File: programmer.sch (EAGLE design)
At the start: 23 parts, among them IC1 74241, U1 ATMEGA8U2, X2 SPARKFUN_USB-MICROB, Y1 16MHz

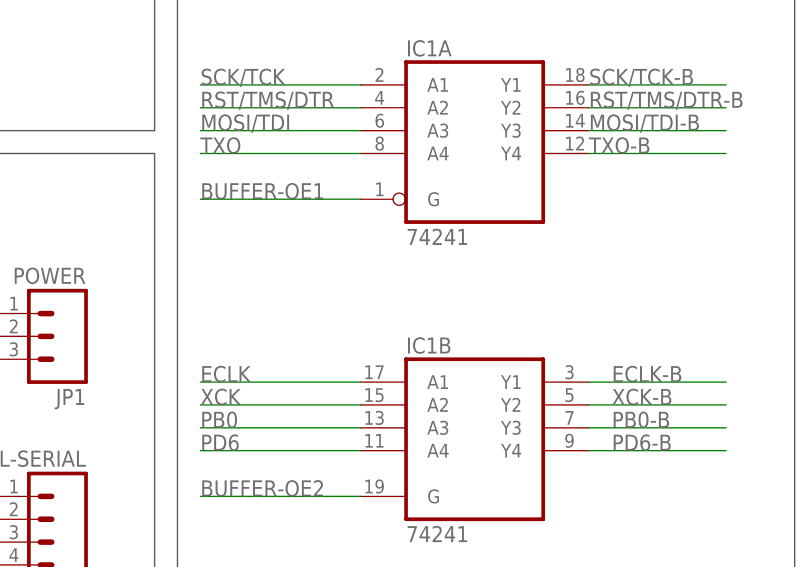
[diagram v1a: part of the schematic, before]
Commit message: Add note about substituting '244.
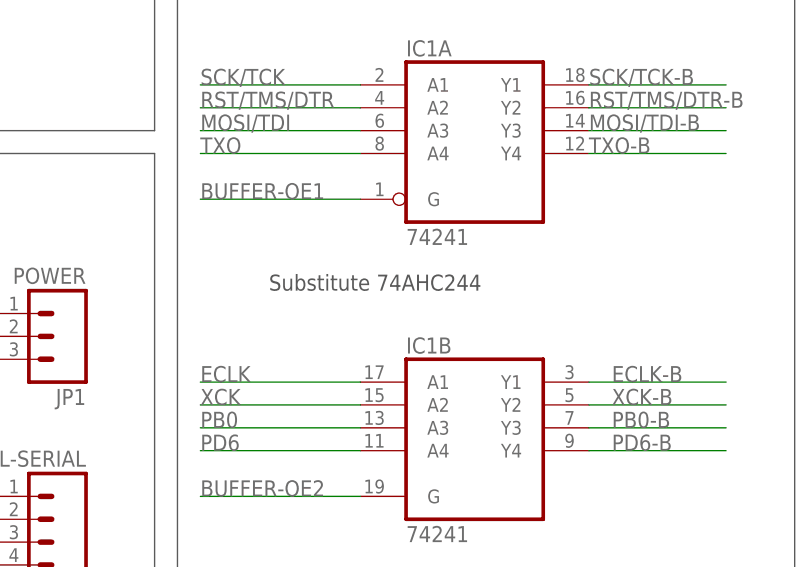
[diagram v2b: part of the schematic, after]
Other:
- note added: "Substitute 74AHC244"
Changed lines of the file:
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@@
 <text x="10.16" y="132.08" size="5.08" layer="97" font="vector">ATmegaXXU2</text>
 <text x="15.24" y="-27.94" size="1.778" layer="97" font="vector">Micro USB connector might not exist in real life</text>
+<text x="109.22" y="38.1" size="1.778" layer="97" font="vector">Substitute 74AHC244</text>
 </plain>
 <instances>

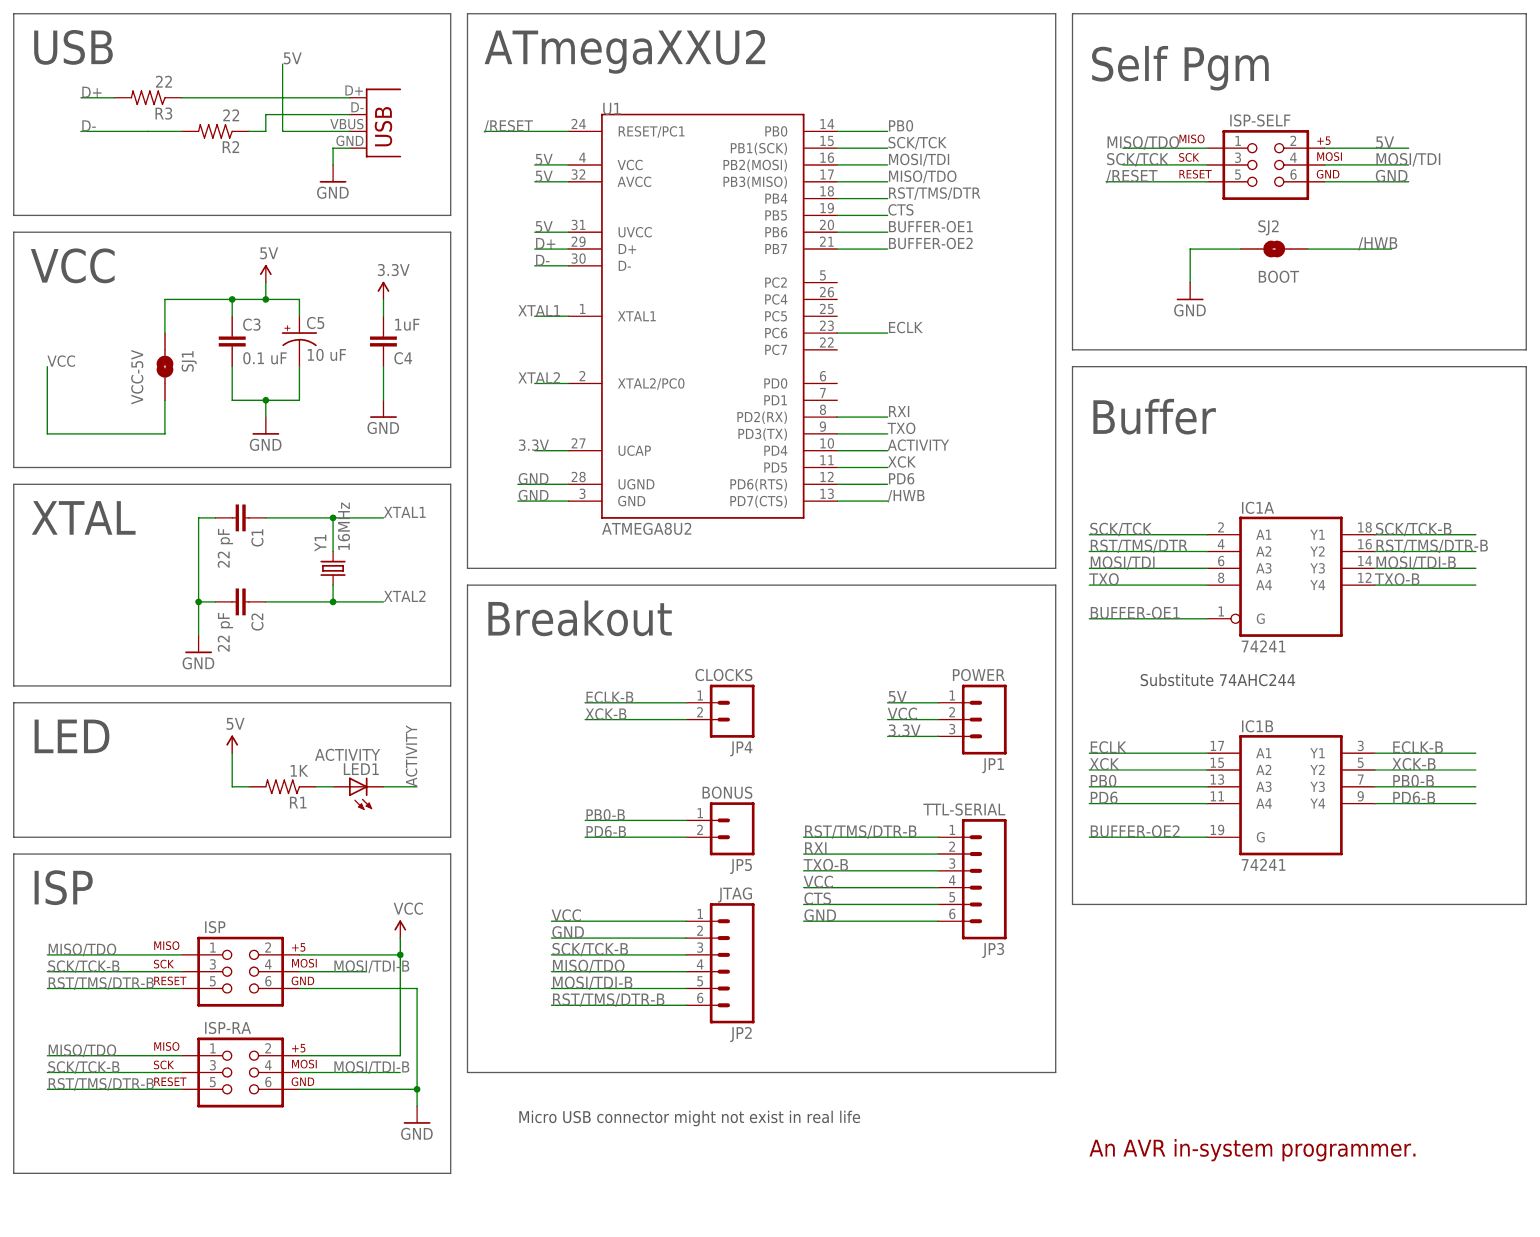
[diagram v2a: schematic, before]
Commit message: Various changes.
- Change VCC labels to VIO (https://github.com/sowbug/avr-programmer/issues/15).
- Change LED resistor from 1K to 330 (https://github.com/sowbug/avr-programmer/issues/16).
- Added second status LED (https://github.com/sowbug/avr-programmer/issues/9).
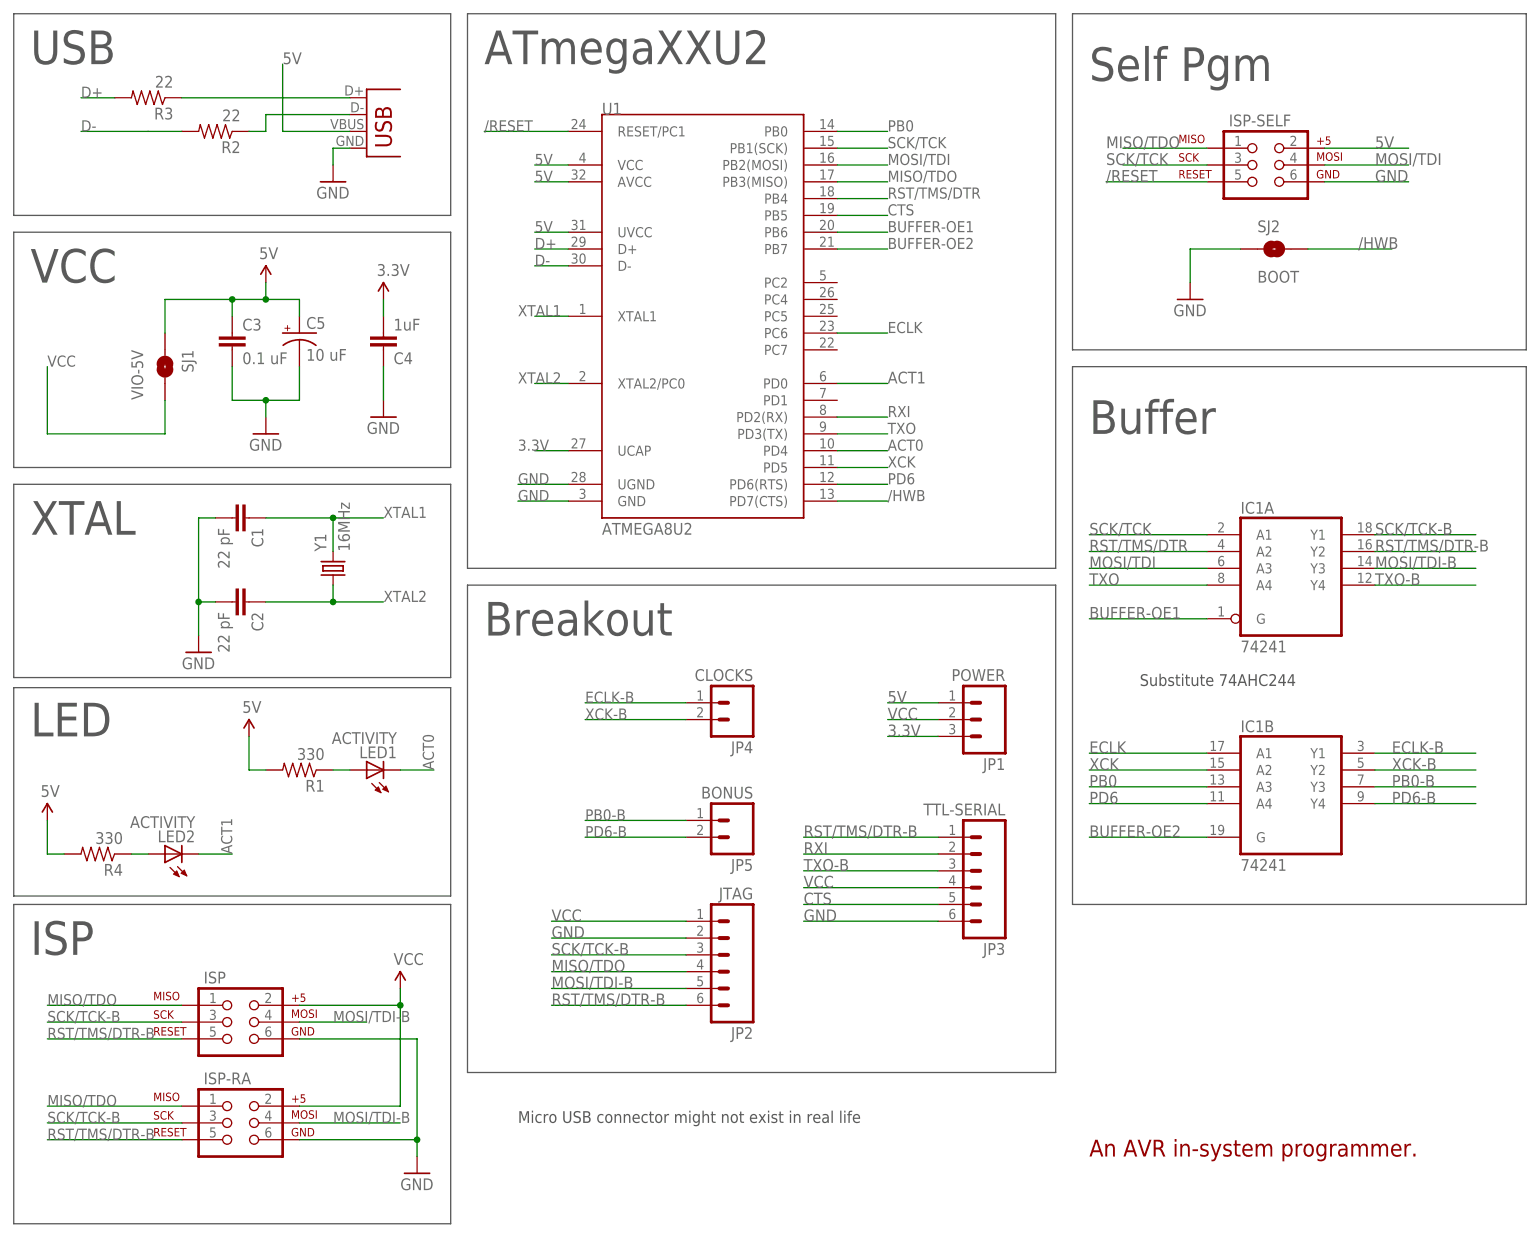
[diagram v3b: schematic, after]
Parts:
- added LED2: ACTIVITY, programmer:SPARKFUN_LED
- added R4: 330, programmer:SPARKFUN_RESISTOR0805-RES
- R1: value 1K -> 330
- SJ1: value VCC-5V -> VIO-5V
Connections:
- net ACTIVITY renamed ACT0
- new net ACT1: LED2.C, U1.PD0
- new net VCC-LED1: LED2.A, R4.1
- net 5V: now also R4.2
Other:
- moved on the sheet: ISP, ISP-RA, LED1, R1

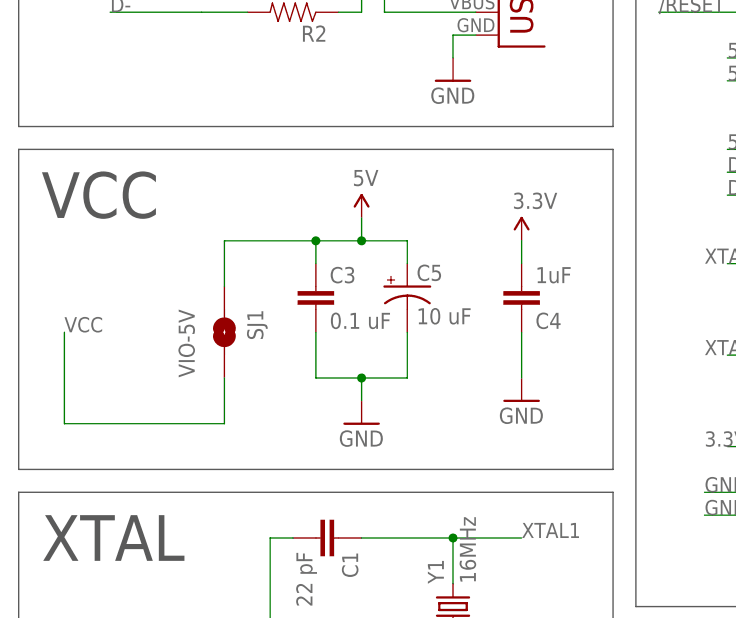
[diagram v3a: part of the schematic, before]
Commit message: Add SJ3 for 3V3 -> VIO.
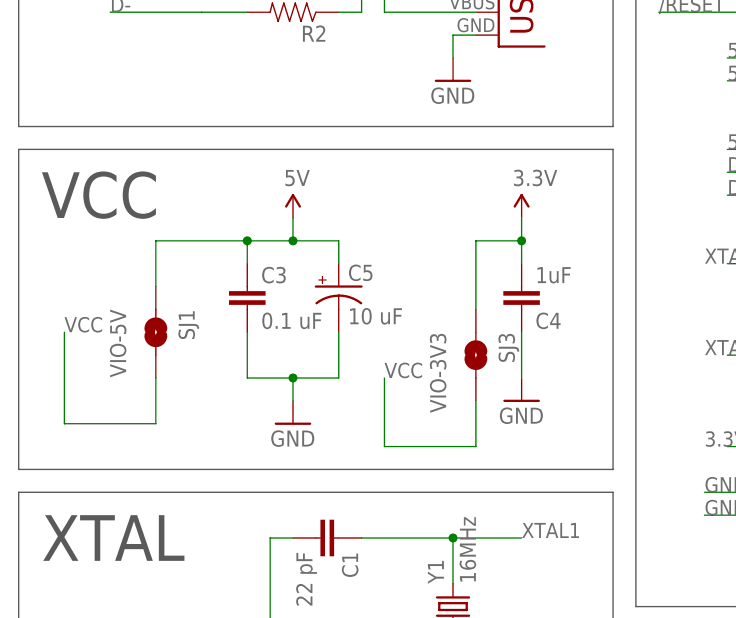
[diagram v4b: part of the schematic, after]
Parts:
- added SJ3: VIO-3V3, programmer:SPARKFUN_SOLDERJUMPERNC
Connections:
- net 3.3V: now also SJ3.1
- net VCC: now also SJ3.2
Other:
- moved on the sheet: C3, C5, SJ1
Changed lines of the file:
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@@
 <part name="U$2" library="SparkFun" deviceset="5V" device=""/>
 <part name="LED2" library="programmer" deviceset="SPARKFUN_LED" device="" value="ACTIVITY"/>
+<part name="SJ3" library="programmer" deviceset="SPARKFUN_SOLDERJUMPER" device="NC" value="VIO-3V3"/>
 </parts>
 <sheets>
@@
 <instance part="C1" gate="G$1" x="-27.94" y="63.5" rot="R270"/>
 <instance part="C2" gate="G$1" x="-27.94" y="50.8" rot="R270"/>
-<instance part="C3" gate="G$1" x="-27.94" y="88.9"/>
-<instance part="GND2" gate="1" x="-22.86" y="76.2"/>
+<instance part="C3" gate="G$1" x="-35.56" y="88.9"/>
+<instance part="GND2" gate="1" x="-30.48" y="76.2"/>
 <instance part="GND3" gate="1" x="-33.02" y="43.18"/>
 <instance part="GND5" gate="1" x="0" y="-35.56"/>
@@
 <instance part="R2" gate="G$1" x="-30.48" y="121.92" rot="R180"/>
 <instance part="C4" gate="G$1" x="-5.08" y="91.44" rot="MR180"/>
-<instance part="P+5" gate="G$1" x="-5.08" y="96.52"/>
+<instance part="P+5" gate="G$1" x="-5.08" y="99.06"/>
 <instance part="FRAME1" gate="G$1" x="-73.66" y="-63.5"/>
 <instance part="FRAME1" gate="G$2" x="99.06" y="-63.5"/>
 <instance part="GND6" gate="1" x="-12.7" y="114.3"/>
 <instance part="R1" gate="G$1" x="-17.78" y="25.4" rot="R180"/>
-<instance part="C5" gate="G$1" x="-17.78" y="91.44"/>
+<instance part="C5" gate="G$1" x="-25.4" y="91.44"/>
 <instance part="GND1" gate="1" x="-5.08" y="78.74"/>
-<instance part="U$1" gate="G$1" x="-22.86" y="99.06"/>
+<instance part="U$1" gate="G$1" x="-30.48" y="99.06"/>
 <instance part="U$3" gate="G$1" x="-25.4" y="30.48"/>
 <instance part="ISP" gate="G$1" x="-27.94" y="-12.7"/>
@@
 <instance part="ISP-SELF" gate="G$1" x="127" y="116.84"/>
 <instance part="X2" gate="G$1" x="-7.62" y="119.38"/>
-<instance part="SJ1" gate="1" x="-38.1" y="86.36" rot="R270"/>
+<instance part="SJ1" gate="1" x="-45.72" y="86.36" rot="R270"/>
 <instance part="JP2" gate="G$1" x="45.72" y="-2.54" rot="R180"/>
 <instance part="JP3" gate="G$1" x="83.82" y="10.16" rot="R180"/>
@@
 <instance part="U$2" gate="G$1" x="-55.88" y="17.78"/>
 <instance part="LED2" gate="G$1" x="-38.1" y="12.7" rot="R90"/>
+<instance part="SJ3" gate="1" x="-10.16" y="83.82" rot="R270"/>
 </instances>
 <busses>
@@
 <segment>
 <wire x1="-55.88" y1="86.36" x2="-55.88" y2="76.2" width="0.1524" layer="91"/>
-<wire x1="-55.88" y1="76.2" x2="-38.1" y2="76.2" width="0.1524" layer="91"/>
-<wire x1="-38.1" y1="76.2" x2="-38.1" y2="81.28" width="0.1524" layer="91"/>
+<wire x1="-55.88" y1="76.2" x2="-45.72" y2="76.2" width="0.1524" layer="91"/>
+<wire x1="-45.72" y1="76.2" x2="-45.72" y2="81.28" width="0.1524" layer="91"/>
 <label x="-55.88" y="86.36" size="1.6764" layer="95" font="vector"/>
 <pinref part="SJ1" gate="1" pin="2"/>
@@
 <label x="58.42" y="7.62" size="1.778" layer="95" font="vector"/>
 </segment>
+<segment>
+<wire x1="-20.32" y1="81.28" x2="-20.32" y2="73.66" width="0.1524" layer="91"/>
+<wire x1="-20.32" y1="73.66" x2="-10.16" y2="73.66" width="0.1524" layer="91"/>
+<wire x1="-10.16" y1="73.66" x2="-10.16" y2="78.74" width="0.1524" layer="91"/>
+<label x="-20.32" y="81.28" size="1.6764" layer="95" font="vector"/>
+<pinref part="SJ3" gate="1" pin="2"/>
+</segment>
 </net>
 <net name="GND" class="1">
@@
 <segment>
 <pinref part="C5" gate="G$1" pin="-"/>
-<wire x1="-17.78" y1="81.28" x2="-17.78" y2="86.36" width="0.1524" layer="91"/>
+<wire x1="-25.4" y1="81.28" x2="-25.4" y2="86.36" width="0.1524" layer="91"/>
 <pinref part="C3" gate="G$1" pin="2"/>
-<wire x1="-27.94" y1="86.36" x2="-27.94" y2="81.28" width="0.1524" layer="91"/>
-<wire x1="-27.94" y1="81.28" x2="-22.86" y2="81.28" width="0.1524" layer="91"/>
+<wire x1="-35.56" y1="86.36" x2="-35.56" y2="81.28" width="0.1524" layer="91"/>
+<wire x1="-35.56" y1="81.28" x2="-30.48" y2="81.28" width="0.1524" layer="91"/>
 <pinref part="GND2" gate="1" pin="GND"/>
-<wire x1="-22.86" y1="81.28" x2="-17.78" y2="81.28" width="0.1524" layer="91"/>
-<wire x1="-22.86" y1="81.28" x2="-22.86" y2="78.74" width="0.1524" layer="91"/>
-<junction x="-22.86" y="81.28"/>
+<wire x1="-30.48" y1="81.28" x2="-25.4" y2="81.28" width="0.1524" layer="91"/>
+<wire x1="-30.48" y1="81.28" x2="-30.48" y2="78.74" width="0.1524" layer="91"/>
+<junction x="-30.48" y="81.28"/>
 </segment>
 <segment>
@@
 <pinref part="P+5" gate="G$1" pin="3.3V"/>
 <wire x1="-5.08" y1="93.98" x2="-5.08" y2="96.52" width="0.1524" layer="91"/>
+<wire x1="-5.08" y1="96.52" x2="-5.08" y2="99.06" width="0.1524" layer="91"/>
+<wire x1="-5.08" y1="96.52" x2="-10.16" y2="96.52" width="0.1524" layer="91"/>
+<wire x1="-10.16" y1="96.52" x2="-10.16" y2="88.9" width="0.1524" layer="91"/>
+<pinref part="SJ3" gate="1" pin="1"/>
+<junction x="-5.08" y="96.52"/>
 </segment>
 <segment>
@@
 <segment>
 <pinref part="C5" gate="G$1" pin="+"/>
-<wire x1="-17.78" y1="96.52" x2="-17.78" y2="93.98" width="0.1524" layer="91"/>
+<wire x1="-25.4" y1="96.52" x2="-25.4" y2="93.98" width="0.1524" layer="91"/>
 <pinref part="C3" gate="G$1" pin="1"/>
-<wire x1="-27.94" y1="93.98" x2="-27.94" y2="96.52" width="0.1524" layer="91"/>
-<wire x1="-27.94" y1="96.52" x2="-22.86" y2="96.52" width="0.1524" layer="91"/>
-<wire x1="-22.86" y1="96.52" x2="-17.78" y2="96.52" width="0.1524" layer="91"/>
-<wire x1="-22.86" y1="99.06" x2="-22.86" y2="96.52" width="0.1524" layer="91"/>
-<junction x="-22.86" y="96.52"/>
+<wire x1="-35.56" y1="93.98" x2="-35.56" y2="96.52" width="0.1524" layer="91"/>
+<wire x1="-35.56" y1="96.52" x2="-30.48" y2="96.52" width="0.1524" layer="91"/>
+<wire x1="-30.48" y1="96.52" x2="-25.4" y2="96.52" width="0.1524" layer="91"/>
+<wire x1="-30.48" y1="99.06" x2="-30.48" y2="96.52" width="0.1524" layer="91"/>
+<junction x="-30.48" y="96.52"/>
 <pinref part="U$1" gate="G$1" pin="5V"/>
-<wire x1="-27.94" y1="96.52" x2="-38.1" y2="96.52" width="0.1524" layer="91"/>
-<wire x1="-38.1" y1="96.52" x2="-38.1" y2="91.44" width="0.1524" layer="91"/>
+<wire x1="-35.56" y1="96.52" x2="-45.72" y2="96.52" width="0.1524" layer="91"/>
+<wire x1="-45.72" y1="96.52" x2="-45.72" y2="91.44" width="0.1524" layer="91"/>
 <pinref part="SJ1" gate="1" pin="1"/>
-<junction x="-27.94" y="96.52"/>
-</segment>
-<segment>
+<junction x="-35.56" y="96.52"/>
+</segment>
+<segment>
